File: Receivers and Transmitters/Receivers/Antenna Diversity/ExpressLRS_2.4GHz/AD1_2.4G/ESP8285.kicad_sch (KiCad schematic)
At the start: 24 parts, among them U3 ESP8285H16, Y2 26MHz

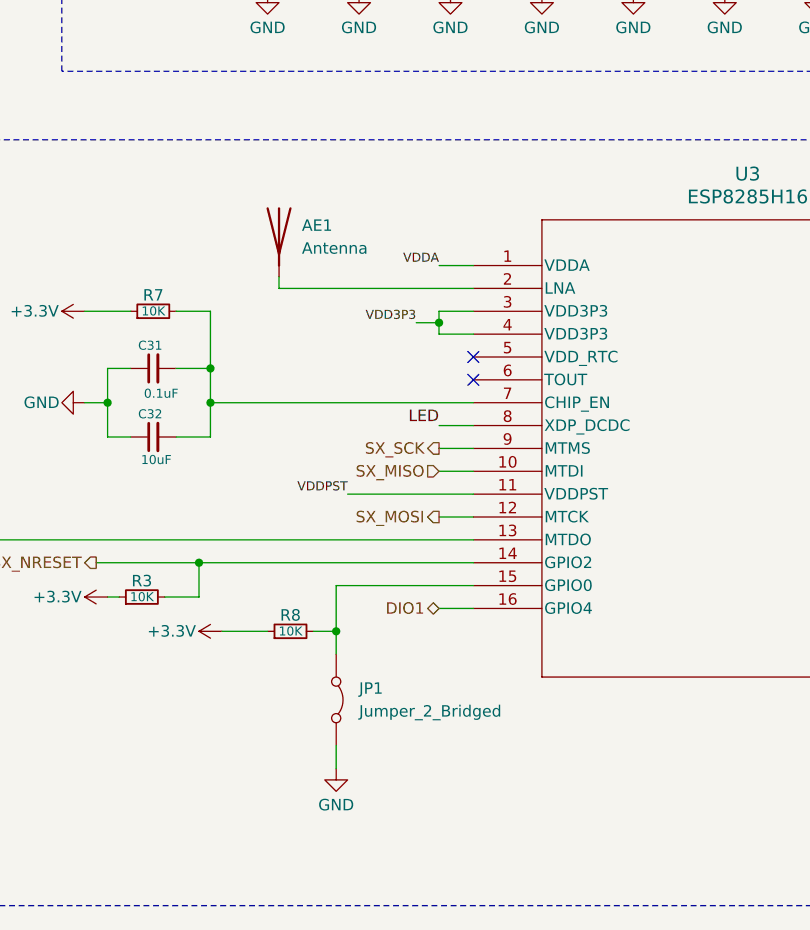
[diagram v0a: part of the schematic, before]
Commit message: Update Antenna Diversity (AD1_2.4G), True Antenna Diversity (TD1_2.4G), and Gemini Mode transmitter (G_TX1): Modify KiCad files, add BOMs and production files; update images, docs, videos, and README; remove outdated Mechanical CAD file
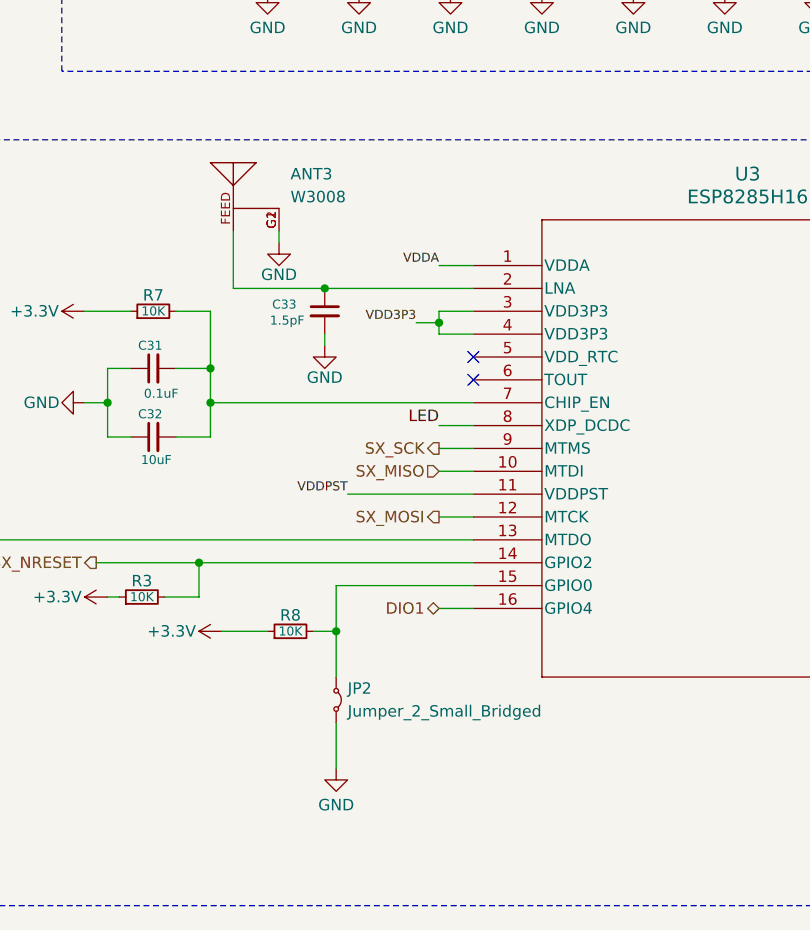
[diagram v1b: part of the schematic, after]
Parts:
- removed AE1: Antenna, RF_Antenna:Texas_SWRA117D_2.4GHz_Right, symbol Device:Antenna
- removed JP1: Jumper_2_Bridged, TestPoint:TestPoint_2Pads_Pitch2.54mm_Drill0.8mm, symbol Jumper:Jumper_2_Bridged
- added ANT3: W3008, W3008:ANTENNA_W3008, symbol W3008:W3008
- added C33: 1.5pF, Capacitor_SMD:C_0402_1005Metric_Pad0.74x0.62mm_HandSolder, symbol Device:C_Small
- added JP2: Jumper_2_Small_Bridged, TestPoint:TestPoint_2Pads_Pitch2.54mm_Drill0.8mm, symbol Jumper:Jumper_2_Small_Bridged
- C21, C22, C23, C24, C25, C26, C27, C28, C29, C31: footprint Capacitor_SMD:C_0805_2012Metric_Pad1.18x1.45mm_HandSolder -> Capacitor_SMD:C_0603_1608Metric_Pad1.08x0.95mm_HandSolder
- D1: footprint LED_SMD:LED_0805_2012Metric_Pad1.15x1.40mm_HandSolder -> LED_SMD:LED_0603_1608Metric_Pad1.05x0.95mm_HandSolder
- R2, R3, R4, R5, R6, R7, R8: footprint Resistor_SMD:R_0805_2012Metric_Pad1.20x1.40mm_HandSolder -> Resistor_SMD:R_0603_1608Metric_Pad0.98x0.95mm_HandSolder
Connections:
- net GND: now also ANT3.G1, ANT3.G2, C33.2, JP2.2 (B)
- net at R8.2, U3.15 (GPIO0): now also JP2.1 (A)
- net at U3.2 (LNA): now also ANT3.FEED, C33.1
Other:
- company: https://github.com/Paschalis | TeodoraMiu -> https://github.com/Paschalis
